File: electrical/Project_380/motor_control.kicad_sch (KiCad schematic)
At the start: 11 parts, among them J1 FL_Motor, J15 DWN_Motor, J2 RL_Motor, J3 FR_Motor, J4 RR_Motor, Q1 RFD14N05L, Q2 RFD14N05L

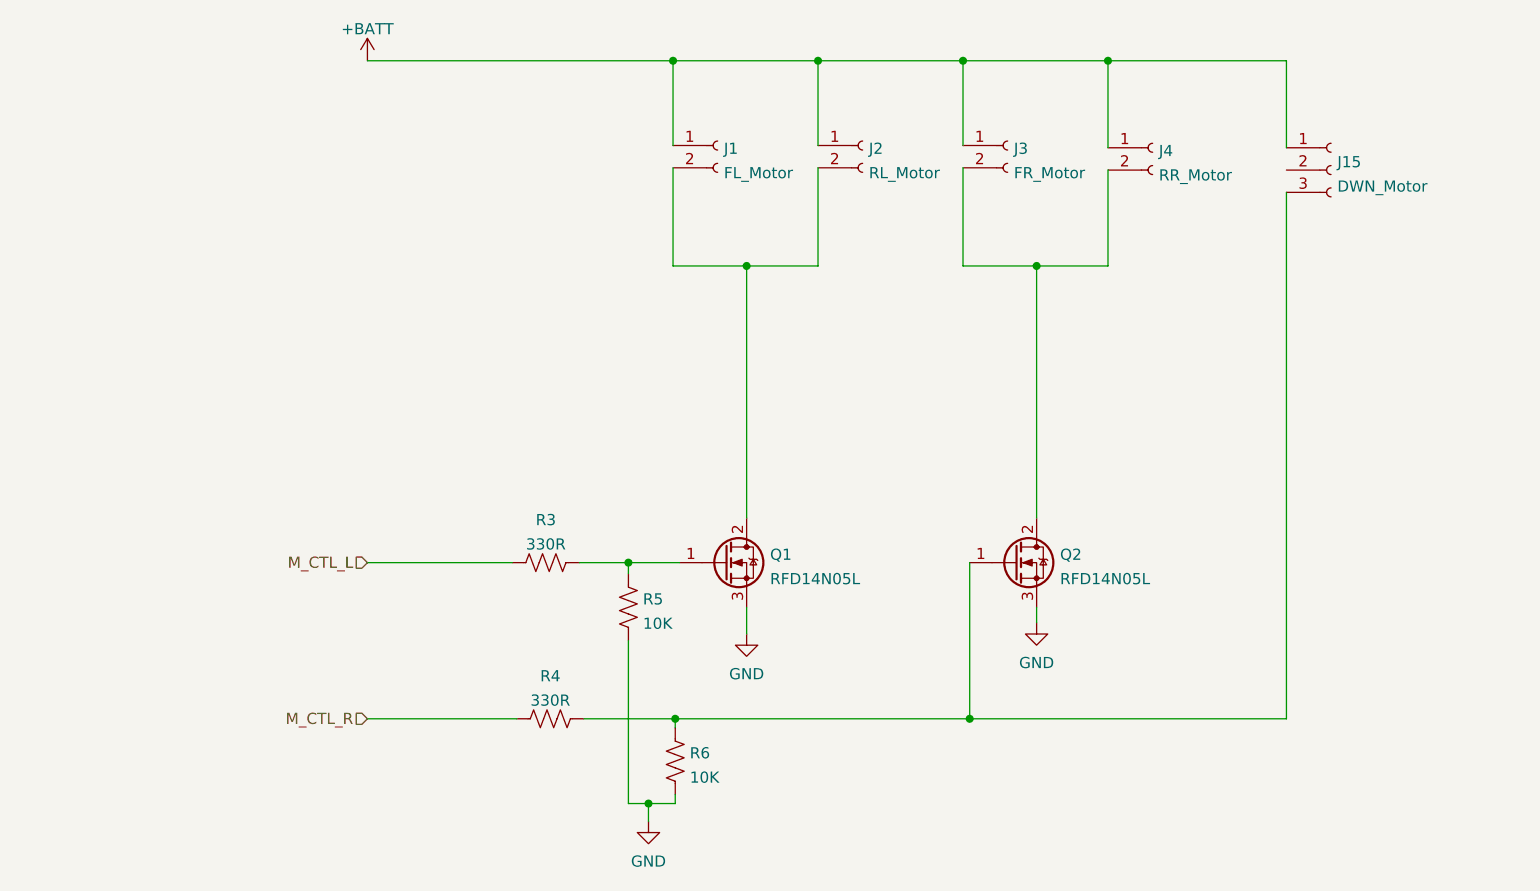
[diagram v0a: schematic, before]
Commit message: added downforce motor control pin
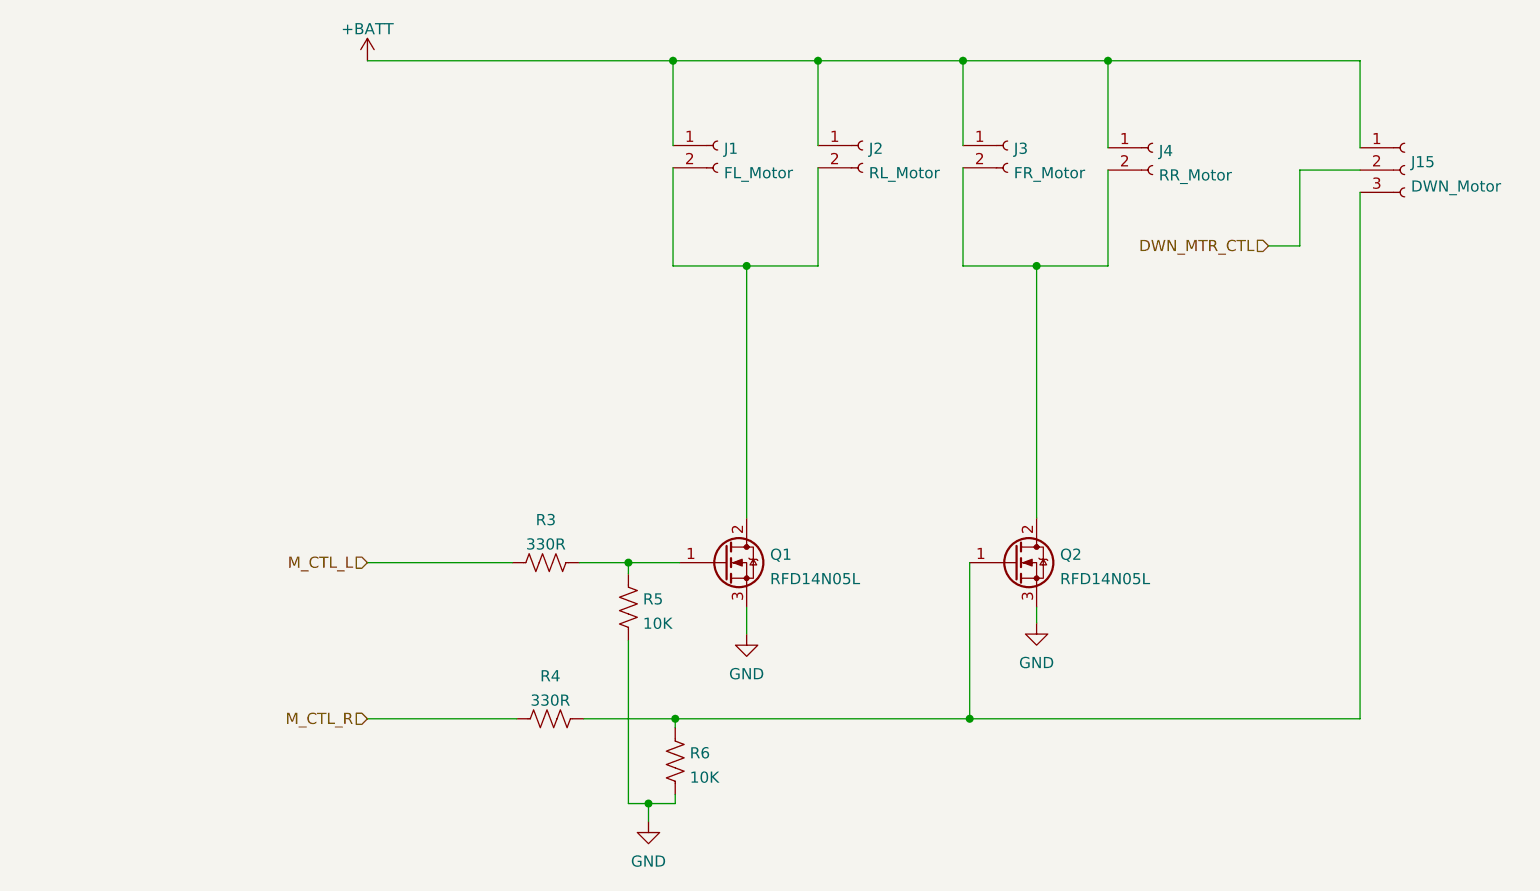
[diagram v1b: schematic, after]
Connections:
- net DWN_MTR_CTL: now reaches J15.2 (Pin_2)
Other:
- title: (none) -> Motor Control
- moved on the sheet: J15
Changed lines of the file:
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@@
 (kicad_sch (version 20211123) (generator eeschema)
   (paper "A4")
+  (title_block
+    (title "Motor Control")
+    (date "2022-02-03")
+    (rev "1.0")
+  )
   (junction (at 177.292 82.55) (diameter 0) (color 0 0 0 0)
   )
@@
     (stroke (width 0) (type default) (color 0 0 0 0))
   )
-  (wire (pts (xy 205.74 59.182) (xy 185.42 59.182))
+  (wire (pts (xy 185.42 59.182) (xy 214.122 59.182))
     (stroke (width 0) (type default) (color 0 0 0 0))
   )
@@
     (stroke (width 0) (type default) (color 0 0 0 0))
   )
-  (wire (pts (xy 205.74 59.182) (xy 205.74 69.088))
-    (stroke (width 0) (type default) (color 0 0 0 0))
-  )
   (wire (pts (xy 135.89 71.374) (xy 135.89 82.55))
     (stroke (width 0) (type default) (color 0 0 0 0))
@@
     (stroke (width 0) (type default) (color 0 0 0 0))
   )
+  (wire (pts (xy 214.122 71.628) (xy 207.264 71.628))
+    (stroke (width 0) (type default) (color 0 0 0 0))
+  )
   (wire (pts (xy 101.092 134.112) (xy 118.11 134.112))
     (stroke (width 0) (type default) (color 0 0 0 0))
@@
     (stroke (width 0) (type default) (color 0 0 0 0))
   )
-  (wire (pts (xy 205.74 134.112) (xy 169.672 134.112))
+  (wire (pts (xy 169.672 134.112) (xy 214.122 134.112))
     (stroke (width 0) (type default) (color 0 0 0 0))
   )
@@
     (stroke (width 0) (type default) (color 0 0 0 0))
   )
+  (wire (pts (xy 207.264 71.628) (xy 207.264 80.264))
+    (stroke (width 0) (type default) (color 0 0 0 0))
+  )
   (wire (pts (xy 168.91 59.182) (xy 168.91 68.834))
     (stroke (width 0) (type default) (color 0 0 0 0))
@@
     (stroke (width 0) (type default) (color 0 0 0 0))
   )
-  (wire (pts (xy 205.74 74.168) (xy 205.74 134.112))
+  (wire (pts (xy 214.122 134.112) (xy 214.122 74.168))
     (stroke (width 0) (type default) (color 0 0 0 0))
   )
@@
     (stroke (width 0) (type default) (color 0 0 0 0))
   )
+  (wire (pts (xy 214.122 69.088) (xy 214.122 59.182))
+    (stroke (width 0) (type default) (color 0 0 0 0))
+  )
+  (wire (pts (xy 203.708 80.264) (xy 207.264 80.264))
+    (stroke (width 0) (type default) (color 0 0 0 0))
+  )
   (wire (pts (xy 136.144 142.748) (xy 136.144 143.764))
     (stroke (width 0) (type default) (color 0 0 0 0))
   )
   (hierarchical_label "M_CTL_R" (shape input) (at 101.092 134.112 180)
+    (effects (font (size 1.27 1.27)) (justify right))
+  )
+  (hierarchical_label "DWN_MTR_CTL" (shape input) (at 203.708 80.264 180)
     (effects (font (size 1.27 1.27)) (justify right))
   )
@@
     (pin "3")
   )
-  (symbol (lib_id "Connector:Conn_01x03_Female") (at 210.82 71.628 0) (unit 1)
-    (in_bom yes) (on_board yes) (fields_autoplaced)
-    (property "Reference" "J15" (id 0) (at 211.5312 70.7195 0)
-      (effects (font (size 1.27 1.27)) (justify left))
-    )
-    (property "Value" "DWN_Motor" (id 1) (at 211.5312 73.4946 0)
-      (effects (font (size 1.27 1.27)) (justify left))
-    )
-    (property "Footprint" "" (id 2) (at 210.82 71.628 0)
-      (effects (font (size 1.27 1.27)) hide)
-    )
-    (property "Datasheet" "~" (id 3) (at 210.82 71.628 0)
-      (effects (font (size 1.27 1.27)) hide)
-    )
+  (symbol (lib_id "Connector:Conn_01x03_Female") (at 219.202 71.628 0) (unit 1)
+    (in_bom yes) (on_board yes) (fields_autoplaced)
+    (property "Reference" "J15" (id 0) (at 219.9132 70.7195 0)
+      (effects (font (size 1.27 1.27)) (justify left))
+    )
+    (property "Value" "DWN_Motor" (id 1) (at 219.9132 73.4946 0)
+      (effects (font (size 1.27 1.27)) (justify left))
+    )
+    (property "Footprint" "" (id 2) (at 219.202 71.628 0)
+      (effects (font (size 1.27 1.27)) hide)
+    )
+    (property "Datasheet" "~" (id 3) (at 219.202 71.628 0)
+      (effects (font (size 1.27 1.27)) hide)
+    )

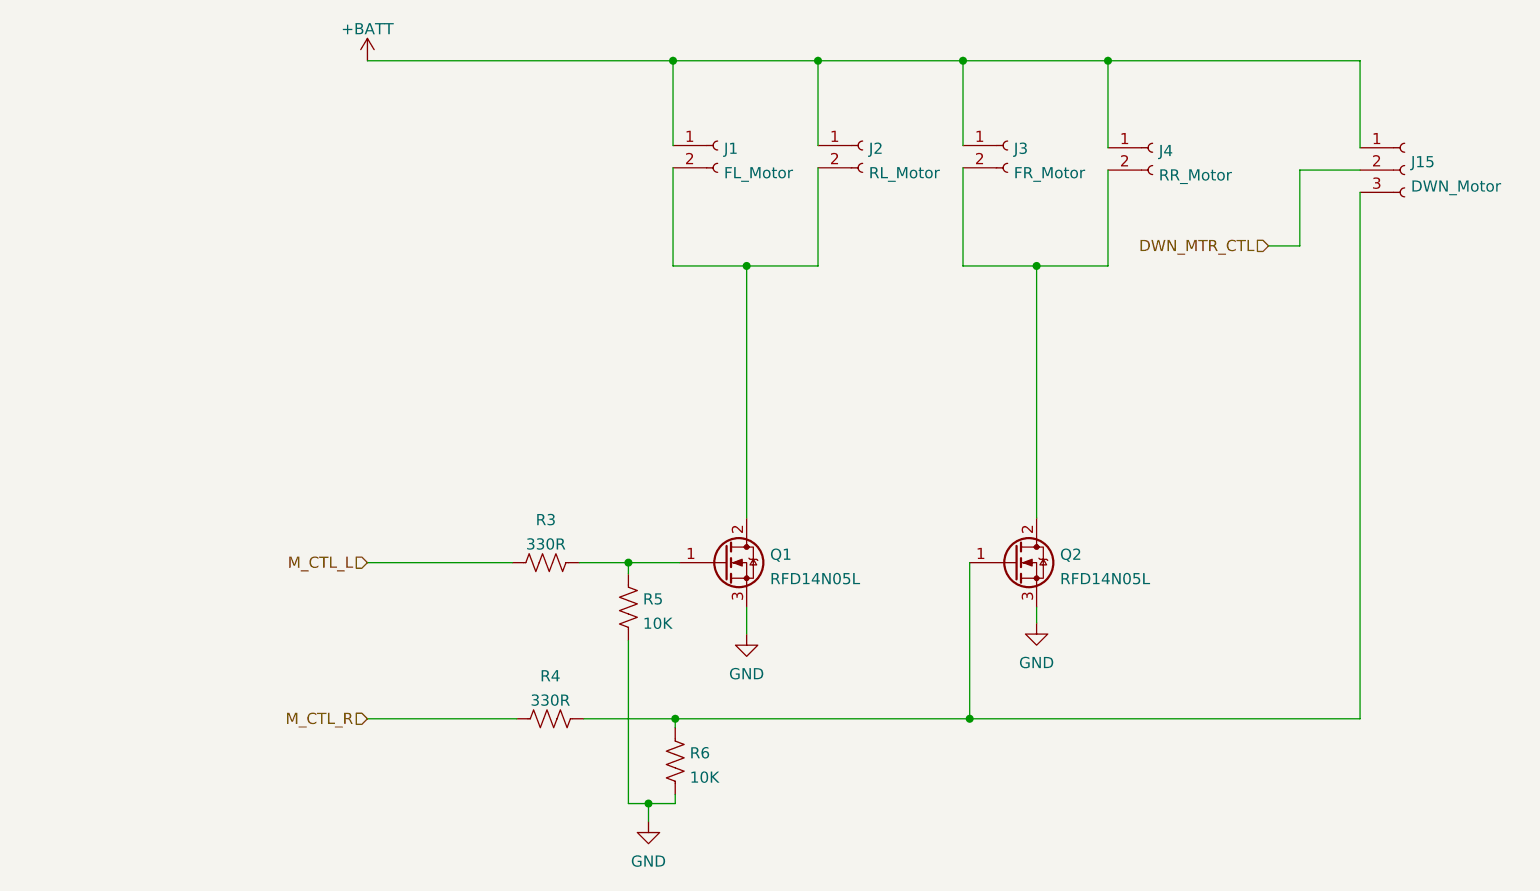
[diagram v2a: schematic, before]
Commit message: added motor controller
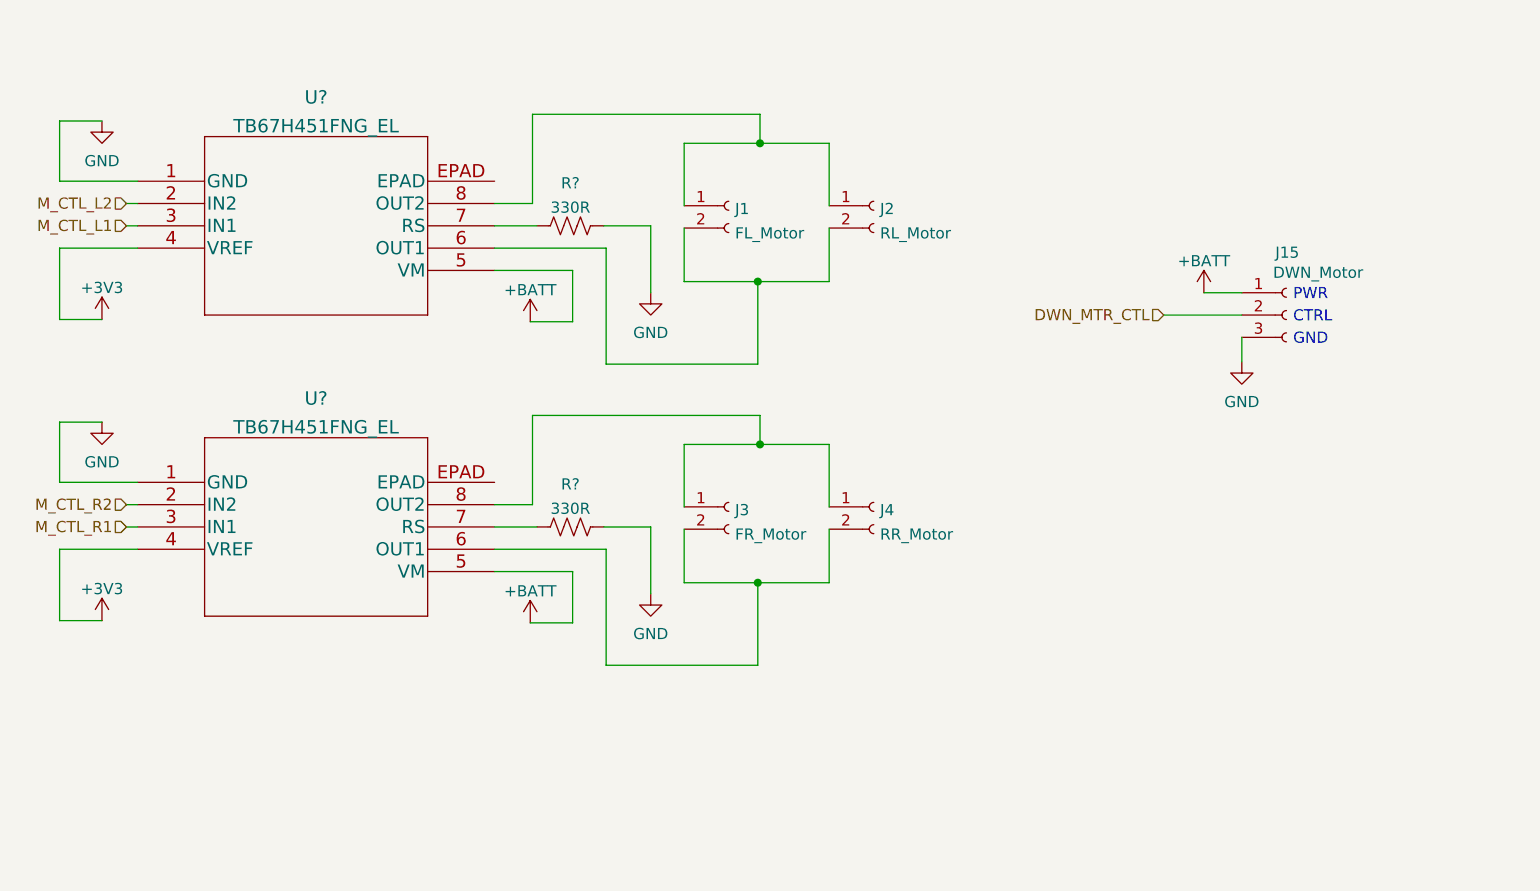
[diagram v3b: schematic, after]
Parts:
- removed Q1, Q2: RFD14N05L, symbol Device:Q_NMOS_GDS
- removed R3, R4: 330R, symbol Device:R_US
- removed R5, R6: 10K, symbol Device:R_US
- added R? (x2): 330R, Resistor_SMD:R_0603_1608Metric, symbol Device:R_US
- added U? (x2): TB67H451FNG_EL, P-HSOP8-0405-1p27-002_TOS, symbol 2022-02-23_19-28-06:TB67H451FNG_EL
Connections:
- net +BATT: now also U?.5 (VM), U?.5 (VM); no longer J1.1 (Pin_1), J2.1 (Pin_1), J3.1 (Pin_1), J4.1 (Pin_1)
- net GND: now also J15.3 (Pin_3), R?.1, R?.1, U?.1 (GND), U?.1 (GND)
- net at J3.2 (Pin_2), J4.2 (Pin_2): now also U?.6 (OUT1)
- net at J1.2 (Pin_2), J2.2 (Pin_2): now also U?.6 (OUT1)
- new net: J3.1 (Pin_1), J4.1 (Pin_1), U?.8 (OUT2)
- new net: R?.2, U?.7 (RS) (x2)
- new net: J1.1 (Pin_1), J2.1 (Pin_1), U?.8 (OUT2)
- new net +3V3: U?.4 (VREF), U?.4 (VREF)
- new net M_CTL_L1: U?.3 (IN1)
- new net M_CTL_L2: U?.2 (IN2)
- new net M_CTL_R1: U?.3 (IN1)
- new net M_CTL_R2: U?.2 (IN2)
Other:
- note added: "CTRL"
- note added: "GND"
- note added: "PWR"
- moved on the sheet: J1, J15, J2
